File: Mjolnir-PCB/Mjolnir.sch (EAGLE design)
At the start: 14 parts, among them U1 ATTINY85-20PU, U2 L78M09ABDT-TR, X1 USB-A

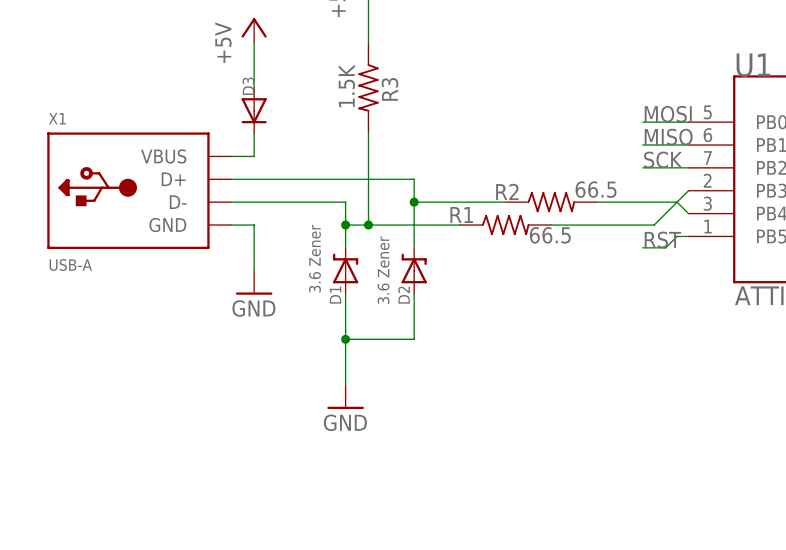
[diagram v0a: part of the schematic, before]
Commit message: Replaced zener diodes to SOD-123 footprint
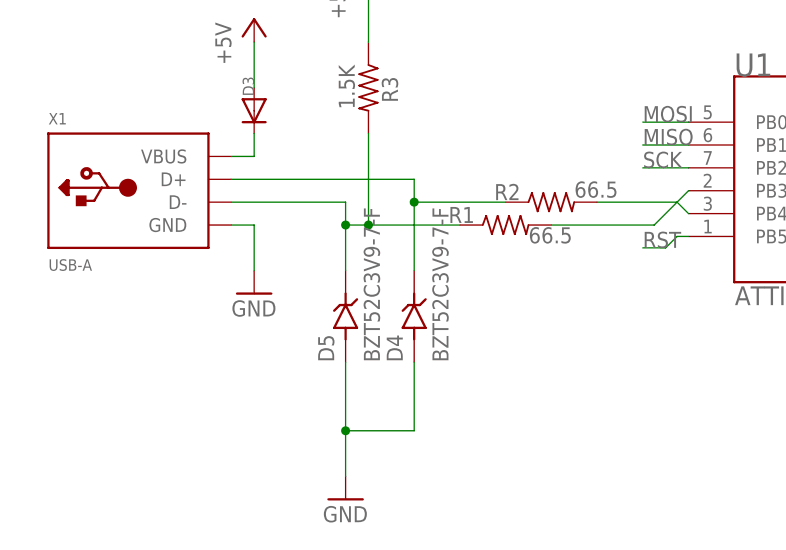
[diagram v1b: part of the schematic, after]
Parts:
- removed D1, D2: 3.6 Zener, microbuilder:DIODE-ZENER
- added D4, D5: BZT52C3V9-7-F, BZT52C3V9-7-F:BZT52C3V9-7-F
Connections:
- net GND: now also D4.A, D5.A; no longer D1.A, D2.A
- net N$3: now also D5.C; no longer D1.C
- net N$5: now also D4.C; no longer D2.C
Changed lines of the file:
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@@
 <part name="U1" library="ATTINY85-20PU" deviceset="ATTINY85-20PU" device=""/>
 <part name="ISP1" library="adafruit" library_urn="urn:adsk.eagle:library:420" deviceset="AVRISP" device="-6" package3d_urn="urn:adsk.eagle:package:6240744/1"/>
-<part name="D1" library="microbuilder" deviceset="DIODE-ZENER" device="" value="3.6 Zener"/>
-<part name="D2" library="microbuilder" deviceset="DIODE-ZENER" device="" value="3.6 Zener"/>
 <part name="R1" library="adafruit" library_urn="urn:adsk.eagle:library:420" deviceset="R-US_" device="R0805" package3d_urn="urn:adsk.eagle:package:6240566/1" value="66.5"/>
 <part name="R2" library="adafruit" library_urn="urn:adsk.eagle:library:420" deviceset="R-US_" device="R0805" package3d_urn="urn:adsk.eagle:package:6240566/1" value="66.5"/>
@@
 <part name="P+6" library="supply1" library_urn="urn:adsk.eagle:library:371" deviceset="+5V" device=""/>
 <part name="P+7" library="supply1" library_urn="urn:adsk.eagle:library:371" deviceset="+5V" device=""/>
+<part name="D4" library="BZT52C3V9-7-F" deviceset="BZT52C3V9-7-F" device=""/>
+<part name="D5" library="BZT52C3V9-7-F" deviceset="BZT52C3V9-7-F" device=""/>
 </parts>
 <sheets>
@@
 <attribute name="NAME" x="53.34" y="40.64" size="1.778" layer="95"/>
 </instance>
-<instance part="D1" gate="G$1" x="7.62" y="5.08" smashed="yes" rot="R90">
-<attribute name="NAME" x="7.1374" y="1.27" size="1.27" layer="95" rot="R90"/>
-<attribute name="VALUE" x="4.8514" y="2.54" size="1.27" layer="96" rot="R90"/>
-</instance>
-<instance part="D2" gate="G$1" x="15.24" y="5.08" smashed="yes" rot="R90">
-<attribute name="NAME" x="14.7574" y="1.27" size="1.27" layer="95" rot="R90"/>
-<attribute name="VALUE" x="12.4714" y="1.27" size="1.27" layer="96" rot="R90"/>
-</instance>
 <instance part="R1" gate="G$1" x="25.4" y="10.16" smashed="yes">
 <attribute name="NAME" x="19.05" y="10.3886" size="1.778" layer="95"/>
@@
 <attribute name="VALUE" x="-5.08" y="0" size="1.778" layer="96"/>
 </instance>
-<instance part="GND4" gate="1" x="7.62" y="-10.16" smashed="yes">
-<attribute name="VALUE" x="5.08" y="-12.7" size="1.778" layer="96"/>
+<instance part="GND4" gate="1" x="7.62" y="-20.32" smashed="yes">
+<attribute name="VALUE" x="5.08" y="-22.86" size="1.778" layer="96"/>
 </instance>
 <instance part="P+3" gate="1" x="10.16" y="38.1" smashed="yes">
@@
 <instance part="P+7" gate="1" x="22.86" y="58.42" smashed="yes" rot="R270">
 <attribute name="VALUE" x="17.78" y="60.96" size="1.778" layer="96"/>
+</instance>
+<instance part="D4" gate="G$1" x="15.24" y="0" smashed="yes" rot="R90">
+<attribute name="NAME" x="13.97" y="-5.08" size="1.778" layer="95" rot="R90"/>
+<attribute name="VALUE" x="19.05" y="-5.08" size="1.778" layer="96" rot="R90"/>
+</instance>
+<instance part="D5" gate="G$1" x="7.62" y="0" smashed="yes" rot="R90">
+<attribute name="NAME" x="6.35" y="-5.08" size="1.778" layer="95" rot="R90"/>
+<attribute name="VALUE" x="11.43" y="-5.08" size="1.778" layer="96" rot="R90"/>
 </instance>
 </instances>
@@
 </segment>
 <segment>
-<pinref part="D1" gate="G$1" pin="A"/>
-<wire x1="7.62" y1="2.54" x2="7.62" y2="-2.54" width="0.1524" layer="91"/>
-<wire x1="15.24" y1="-2.54" x2="7.62" y2="-2.54" width="0.1524" layer="91"/>
-<junction x="7.62" y="-2.54"/>
-<wire x1="7.62" y1="-2.54" x2="7.62" y2="-7.62" width="0.1524" layer="91"/>
+<wire x1="7.62" y1="-5.08" x2="7.62" y2="-12.7" width="0.1524" layer="91"/>
+<wire x1="15.24" y1="-12.7" x2="7.62" y2="-12.7" width="0.1524" layer="91"/>
+<junction x="7.62" y="-12.7"/>
+<wire x1="7.62" y1="-12.7" x2="7.62" y2="-17.78" width="0.1524" layer="91"/>
 <pinref part="GND4" gate="1" pin="GND"/>
-<pinref part="D2" gate="G$1" pin="A"/>
-<wire x1="15.24" y1="2.54" x2="15.24" y2="-2.54" width="0.1524" layer="91"/>
+<wire x1="15.24" y1="-5.08" x2="15.24" y2="-12.7" width="0.1524" layer="91"/>
+<pinref part="D5" gate="G$1" pin="A"/>
+<pinref part="D4" gate="G$1" pin="A"/>
 </segment>
 <segment>
@@
 <wire x1="-5.08" y1="12.7" x2="7.62" y2="12.7" width="0.1524" layer="91"/>
 <wire x1="7.62" y1="12.7" x2="7.62" y2="10.16" width="0.1524" layer="91"/>
-<pinref part="D1" gate="G$1" pin="C"/>
 <pinref part="R1" gate="G$1" pin="1"/>
-<wire x1="7.62" y1="10.16" x2="7.62" y2="7.62" width="0.1524" layer="91"/>
 <wire x1="20.32" y1="10.16" x2="10.16" y2="10.16" width="0.1524" layer="91"/>
 <junction x="7.62" y="10.16"/>
@@
 <junction x="10.16" y="10.16"/>
 <pinref part="R3" gate="G$1" pin="2"/>
+<pinref part="D5" gate="G$1" pin="C"/>
+<wire x1="7.62" y1="5.08" x2="7.62" y2="10.16" width="0.1524" layer="91"/>
 </segment>
 </net>
@@
 <pinref part="X1" gate="G$1" pin="D+"/>
 <wire x1="-5.08" y1="15.24" x2="15.24" y2="15.24" width="0.1524" layer="91"/>
-<pinref part="D2" gate="G$1" pin="C"/>
 <wire x1="15.24" y1="15.24" x2="15.24" y2="12.7" width="0.1524" layer="91"/>
 <pinref part="R2" gate="G$1" pin="1"/>
-<wire x1="15.24" y1="12.7" x2="15.24" y2="7.62" width="0.1524" layer="91"/>
+<wire x1="15.24" y1="12.7" x2="15.24" y2="5.08" width="0.1524" layer="91"/>
 <wire x1="25.4" y1="12.7" x2="15.24" y2="12.7" width="0.1524" layer="91"/>
 <junction x="15.24" y="12.7"/>
-</segment>
-</net>
+<pinref part="D4" gate="G$1" pin="C"/>
+</segment>
+</net>
